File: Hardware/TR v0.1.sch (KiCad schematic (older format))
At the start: 54 parts, among them IC1 ATmega328PB-AU, J1 Input, J2 OutputAll, J3 Delay CV1, J4 Delay CV2, J5 Delay CV3, J6 OutputOne, J7 OutputTwo, J8 OutputThree, Q1 BC847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

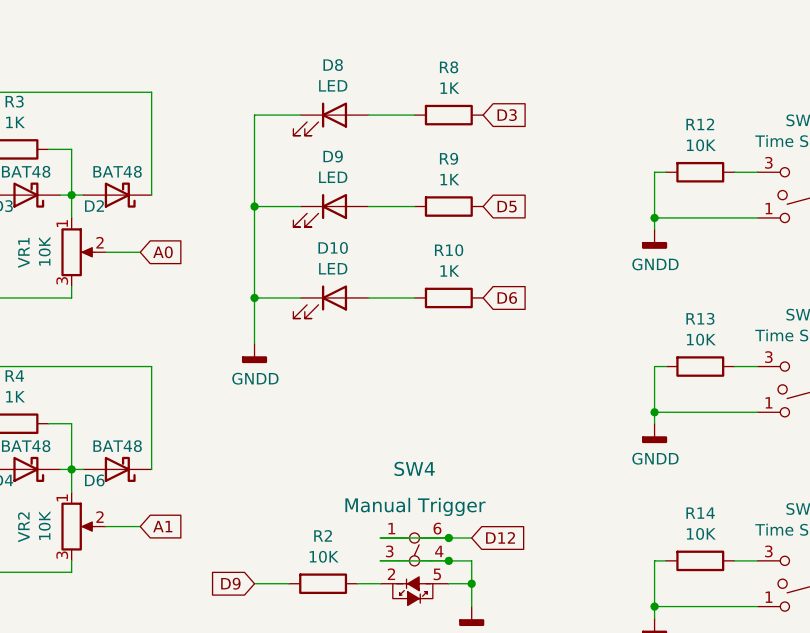
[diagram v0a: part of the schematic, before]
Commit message: Updated Schematic with LED for mode
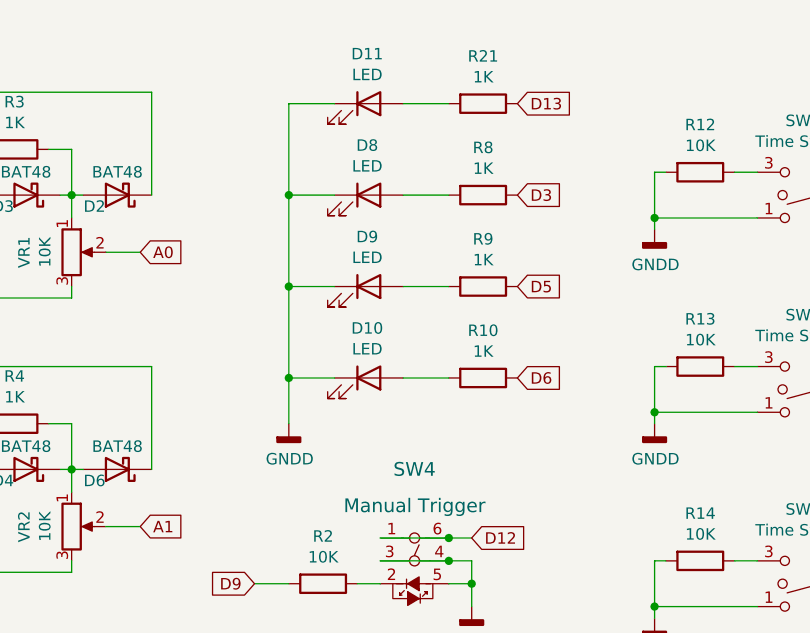
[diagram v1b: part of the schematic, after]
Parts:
- added D11: LED, LED_THT:LED_D3.0mm_FlatTop, symbol Device:LED
- added R21: 1K, Resistor_SMD:R_0603_1608Metric, symbol Device:R
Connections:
- net D13: now also R21.1
- net GNDD: now also D11.1 (K)
- new net: D11.2 (A), R21.2
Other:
- moved on the sheet: D10, D8, D9, R10, R8, R9
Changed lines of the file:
@@
 Wire Wire Line
 	2950 2200 2950 2350
-Connection ~ 6050 1350
-Wire Wire Line
-	6050 1750 6050 1950
-Connection ~ 6050 1750
-Wire Wire Line
-	6050 1350 6050 1750
-Wire Wire Line
-	6050 950  6050 1350
-Wire Wire Line
-	6250 1350 6050 1350
-Wire Wire Line
-	6250 1750 6050 1750
-Wire Wire Line
-	6250 950  6050 950
+Connection ~ 6200 1700
+Wire Wire Line
+	6200 2100 6200 2300
+Connection ~ 6200 2100
+Wire Wire Line
+	6200 1700 6200 2100
+Wire Wire Line
+	6200 1300 6200 1700
+Wire Wire Line
+	6400 1700 6200 1700
+Wire Wire Line
+	6400 2100 6200 2100
+Wire Wire Line
+	6400 1300 6200 1300
 $Comp
 L power:GNDD #PWR021
 U 1 1 6062BBC7
-P 6050 1950
-F 0 "#PWR021" H 6050 1700 50  0001 C CNN
-F 1 "GNDD" H 6054 1795 50  0000 C CNN
-F 2 "" H 6050 1950 50  0001 C CNN
-F 3 "" H 6050 1950 50  0001 C CNN
-	1    6050 1950
+P 6200 2300
+F 0 "#PWR021" H 6200 2050 50  0001 C CNN
+F 1 "GNDD" H 6204 2145 50  0000 C CNN
+F 2 "" H 6200 2300 50  0001 C CNN
+F 3 "" H 6200 2300 50  0001 C CNN
+	1    6200 2300
 	1    0    0    -1
 $EndComp
@@
 L Device:LED D10
 U 1 1 60608AFB
-P 6400 1750
-F 0 "D10" H 6393 1967 50  0000 C CNN
-F 1 "LED" H 6393 1876 50  0000 C CNN
-F 2 "LED_THT:LED_D3.0mm_FlatTop" H 6400 1750 50  0001 C CNN
-F 3 "~" H 6400 1750 50  0001 C CNN
-	1    6400 1750
+P 6550 2100
+F 0 "D10" H 6543 2317 50  0000 C CNN
+F 1 "LED" H 6543 2226 50  0000 C CNN
+F 2 "LED_THT:LED_D3.0mm_FlatTop" H 6550 2100 50  0001 C CNN
+F 3 "~" H 6550 2100 50  0001 C CNN
+	1    6550 2100
 	1    0    0    -1
 $EndComp
@@
 L Device:LED D9
 U 1 1 60608728
-P 6400 1350
-F 0 "D9" H 6393 1567 50  0000 C CNN
-F 1 "LED" H 6393 1476 50  0000 C CNN
-F 2 "LED_THT:LED_D3.0mm_FlatTop" H 6400 1350 50  0001 C CNN
-F 3 "~" H 6400 1350 50  0001 C CNN
-	1    6400 1350
+P 6550 1700
+F 0 "D9" H 6543 1917 50  0000 C CNN
+F 1 "LED" H 6543 1826 50  0000 C CNN
+F 2 "LED_THT:LED_D3.0mm_FlatTop" H 6550 1700 50  0001 C CNN
+F 3 "~" H 6550 1700 50  0001 C CNN
+	1    6550 1700
 	1    0    0    -1
 $EndComp
@@
 L Device:LED D8
 U 1 1 60605992
-P 6400 950
-F 0 "D8" H 6393 1167 50  0000 C CNN
-F 1 "LED" H 6393 1076 50  0000 C CNN
-F 2 "LED_THT:LED_D3.0mm_FlatTop" H 6400 950 50  0001 C CNN
-F 3 "~" H 6400 950 50  0001 C CNN
-	1    6400 950
-	1    0    0    -1
-$EndComp
-Text GLabel 7050 950  2    50   Input ~ 0
+P 6550 1300
+F 0 "D8" H 6543 1517 50  0000 C CNN
+F 1 "LED" H 6543 1426 50  0000 C CNN
+F 2 "LED_THT:LED_D3.0mm_FlatTop" H 6550 1300 50  0001 C CNN
+F 3 "~" H 6550 1300 50  0001 C CNN
+	1    6550 1300
+	1    0    0    -1
+$EndComp
+Text GLabel 7200 1300 2    50   Input ~ 0
 D3
-Text GLabel 7050 1350 2    50   Input ~ 0
+Text GLabel 7200 1700 2    50   Input ~ 0
 D5
-Text GLabel 7050 1750 2    50   Input ~ 0
+Text GLabel 7200 2100 2    50   Input ~ 0
 D6
 $Comp
 L Device:R R10
 U 1 1 607B4949
-P 6900 1750
-F 0 "R10" V 6693 1750 50  0000 C CNN
-F 1 "1K" V 6784 1750 50  0000 C CNN
-F 2 "Resistor_SMD:R_0603_1608Metric" V 6830 1750 50  0001 C CNN
-F 3 "~" H 6900 1750 50  0001 C CNN
-	1    6900 1750
+P 7050 2100
+F 0 "R10" V 6843 2100 50  0000 C CNN
+F 1 "1K" V 6934 2100 50  0000 C CNN
+F 2 "Resistor_SMD:R_0603_1608Metric" V 6980 2100 50  0001 C CNN
+F 3 "~" H 7050 2100 50  0001 C CNN
+	1    7050 2100
 	0    1    1    0
 $EndComp
@@
 L Device:R R9
 U 1 1 607B458A
-P 6900 1350
-F 0 "R9" V 6693 1350 50  0000 C CNN
-F 1 "1K" V 6784 1350 50  0000 C CNN
-F 2 "Resistor_SMD:R_0603_1608Metric" V 6830 1350 50  0001 C CNN
-F 3 "~" H 6900 1350 50  0001 C CNN
-	1    6900 1350
-	0    1    1    0
-$EndComp
-Wire Wire Line
-	6550 1350 6750 1350
-Wire Wire Line
-	6550 950  6750 950
-Wire Wire Line
-	6550 1750 6750 1750
+P 7050 1700
+F 0 "R9" V 6843 1700 50  0000 C CNN
+F 1 "1K" V 6934 1700 50  0000 C CNN
+F 2 "Resistor_SMD:R_0603_1608Metric" V 6980 1700 50  0001 C CNN
+F 3 "~" H 7050 1700 50  0001 C CNN
+	1    7050 1700
+	0    1    1    0
+$EndComp
+Wire Wire Line
+	6700 1700 6900 1700
+Wire Wire Line
+	6700 1300 6900 1300
+Wire Wire Line
+	6700 2100 6900 2100
 $Comp
 L Device:R R8
 U 1 1 605FFAEB
-P 6900 950
-F 0 "R8" V 6693 950 50  0000 C CNN
-F 1 "1K" V 6784 950 50  0000 C CNN
-F 2 "Resistor_SMD:R_0603_1608Metric" V 6830 950 50  0001 C CNN
-F 3 "~" H 6900 950 50  0001 C CNN
-	1    6900 950
+P 7050 1300
+F 0 "R8" V 6843 1300 50  0000 C CNN
+F 1 "1K" V 6934 1300 50  0000 C CNN
+F 2 "Resistor_SMD:R_0603_1608Metric" V 6980 1300 50  0001 C CNN
+F 3 "~" H 7050 1300 50  0001 C CNN
+	1    7050 1300
 	0    1    1    0
 $EndComp
@@
 	0    1    1    0
 $EndComp
+$Comp
+L Device:LED D11
+U 1 1 606E7E1B
+P 6550 900
+F 0 "D11" H 6543 1117 50  0000 C CNN
+F 1 "LED" H 6543 1026 50  0000 C CNN
+F 2 "LED_THT:LED_D3.0mm_FlatTop" H 6550 900 50  0001 C CNN
+F 3 "~" H 6550 900 50  0001 C CNN
+	1    6550 900
+	1    0    0    -1
+$EndComp
+$Comp
+L Device:R R21
+U 1 1 606E829A
+P 7050 900
+F 0 "R21" V 6843 900 50  0000 C CNN
+F 1 "1K" V 6934 900 50  0000 C CNN
+F 2 "Resistor_SMD:R_0603_1608Metric" V 6980 900 50  0001 C CNN
+F 3 "~" H 7050 900 50  0001 C CNN
+	1    7050 900
+	0    1    1    0
+$EndComp
+Text GLabel 7200 900  2    50   Input ~ 0
+D13
+Wire Wire Line
+	6700 900  6900 900
+Wire Wire Line
+	6400 900  6200 900
+Wire Wire Line
+	6200 900  6200 1300
+Connection ~ 6200 1300
 $EndSCHEMATC

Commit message: Analog trigger Input working, Updt License & Sch
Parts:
- Q1: value BC847 -> MMBT3094
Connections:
- net A6: now also Q1.3 (C), R19.1
- net D1: no longer Q1.3 (C), R19.1
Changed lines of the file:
@@
 Connection ~ 8850 3000
 Text GLabel 10900 1400 2    50   Input ~ 0
-D1
+A6
 Wire Wire Line
 	9600 1950 10150 1950
@@
 P 10650 1750
 F 0 "Q1" H 10840 1796 50  0000 L CNN
-F 1 "BC847" H 10840 1705 50  0000 L CNN
+F 1 "MMBT3094" H 10840 1705 50  0000 L CNN
 F 2 "Package_TO_SOT_SMD:SOT-23" H 10850 1675 50  0001 L CIN
 F 3 "https://www.onsemi.com/pub/Collateral/2N3903-D.PDF" H 10650 1750 50  0001 L CNN

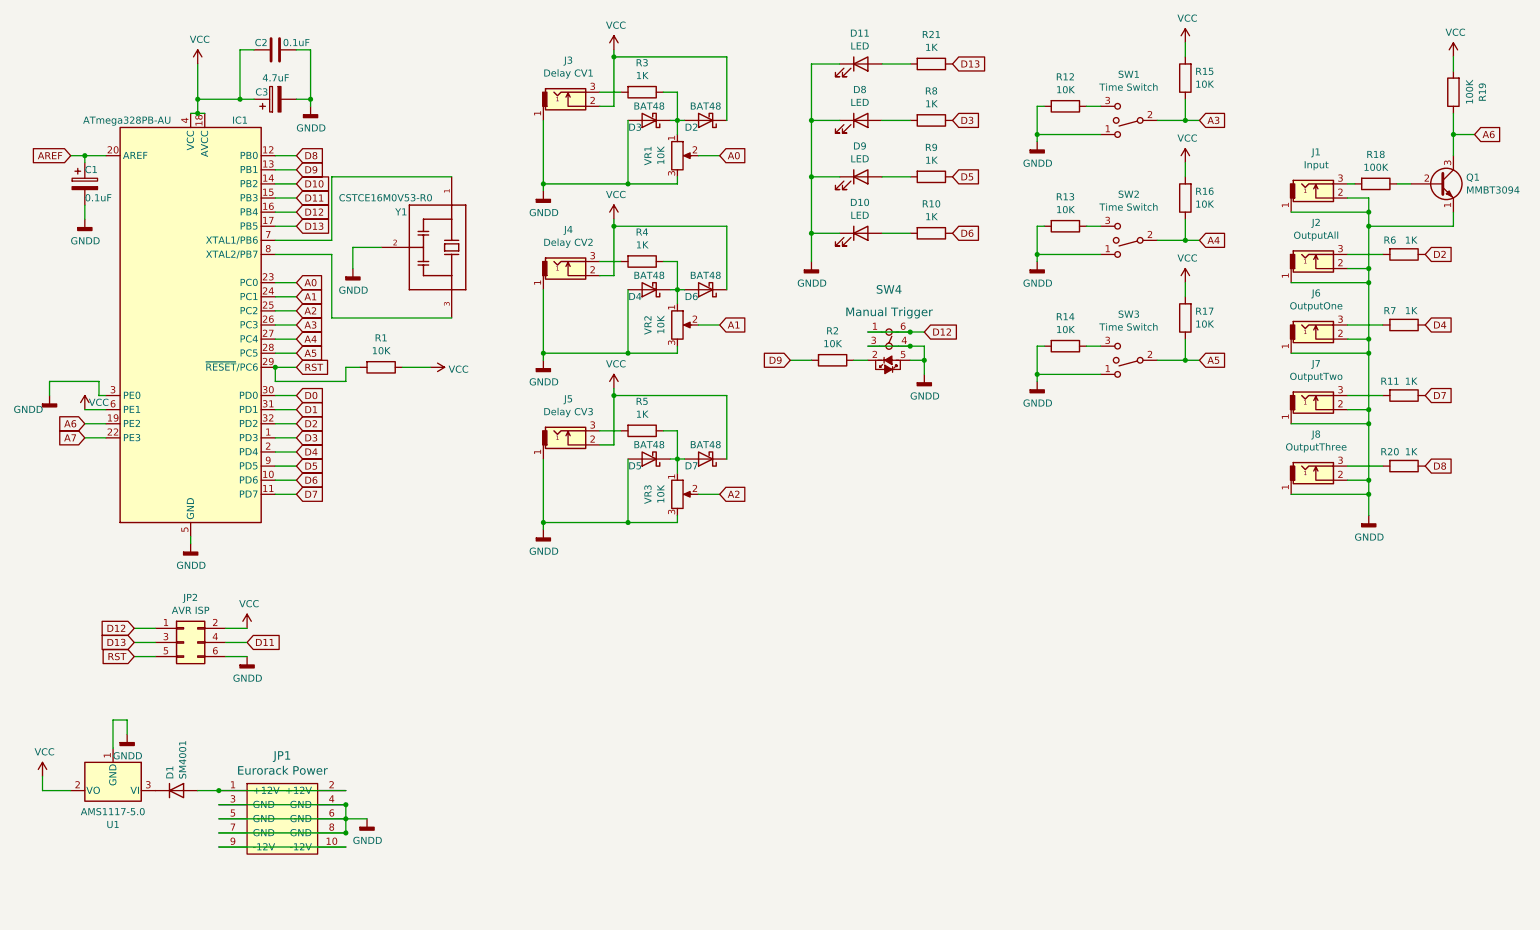
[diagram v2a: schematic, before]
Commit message: Hold button bug, but everything else is alright.
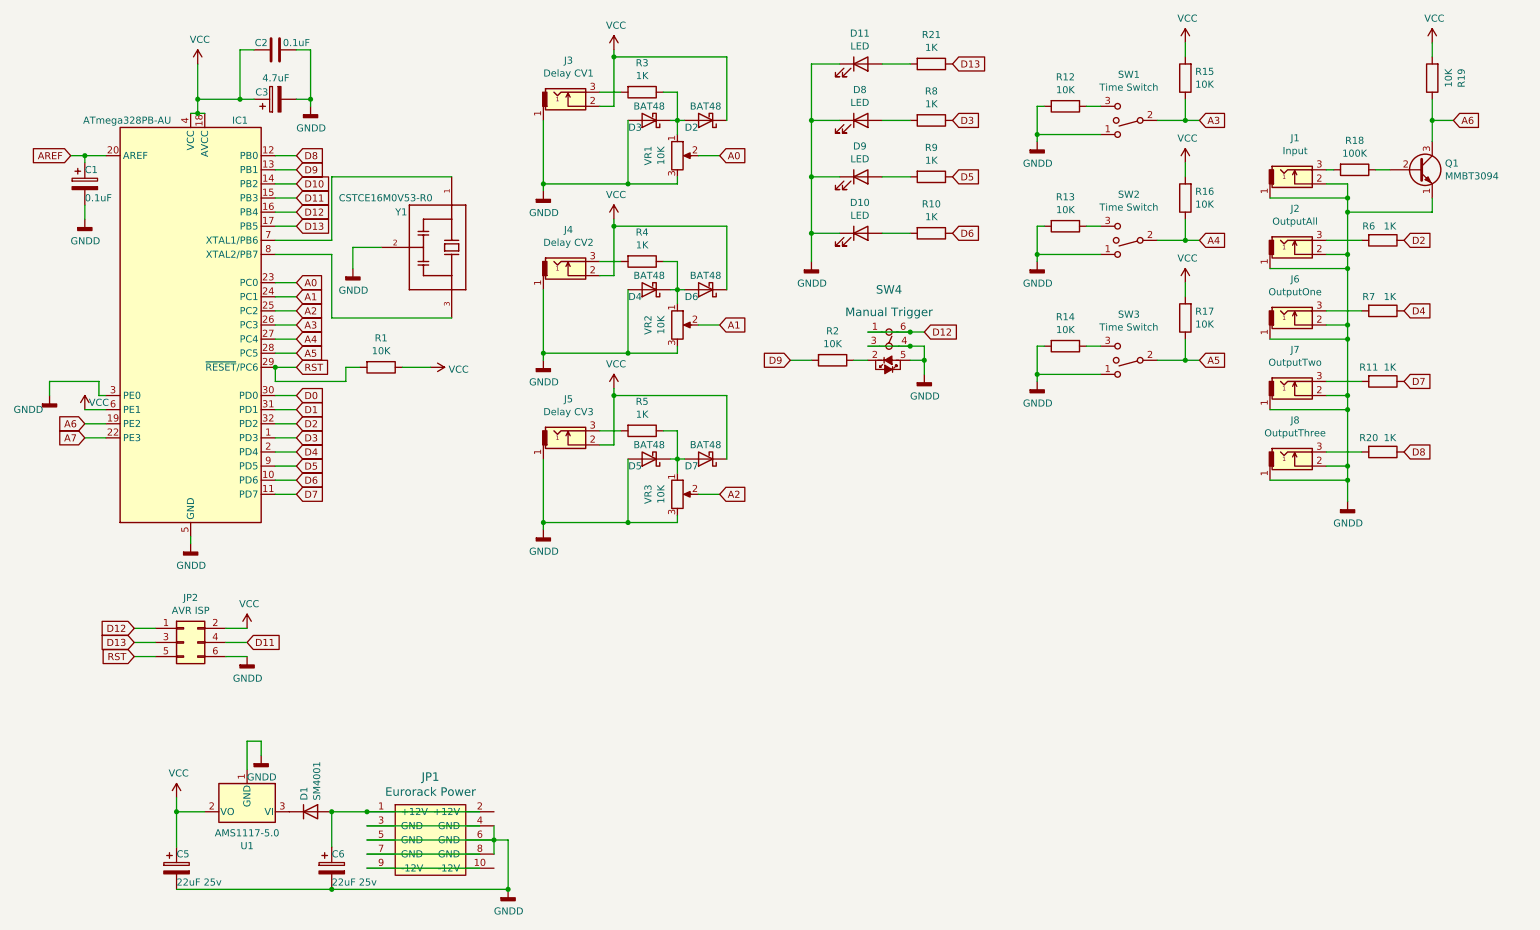
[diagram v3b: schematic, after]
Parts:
- added C5: 22uF 25v, Capacitor_SMD:CP_Elec_5x5.8, symbol Device:CP
- added C6: 22uF 25v, Capacitor_SMD:CP_Elec_3x5.3, symbol Device:CP
- R19: value 100K -> 10K
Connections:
- net GNDD: now also C5.2, C6.2; no longer JP1.3 (GND), JP1.7 (GND)
- net VCC: now also C5.1
- net at D1.2 (A), JP1.1 (+12V): now also C6.1; no longer JP1.2 (+12V)
- net at JP1.10 (-12V): no longer JP1.9 (-12V)
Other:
- moved on the sheet: D1, J1, J2, J6, J7, J8, JP1, Q1, R11, R18, R19, R20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
